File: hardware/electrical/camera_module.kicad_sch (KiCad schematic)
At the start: 19 parts, among them J5 FFC, Q7 AO3401A, U3 TLV70028DCKR, U9 TLV70012DCKR, X2 SG-8018CA 24.0000M-TJHPA3

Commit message: Component selection
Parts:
- C44, C52, C53: footprint (none) -> Capacitor_SMD:C_0402_1005Metric; LCSC Part # (none) -> C1525; Mfr (none) -> Samsung Electro-Mechanics; Mfr. Part # (none) -> CL05B104KO5NNNC
- C45: footprint (none) -> Capacitor_SMD:C_0603_1608Metric; LCSC Part # (none) -> C1644; Mfr (none) -> Samsung Electro-Mechanics; Mfr. Part # (none) -> CL10C150JB8NNNC
- C46, C47, C48, C49: footprint Capacitor_SMD:C_1206_3216Metric -> Capacitor_SMD:C_0402_1005Metric; LCSC Part # (none) -> C52923; Mfr (none) -> Samsung Electro-Mechanics; Mfr. Part # (none) -> CL05A105KA5NQNC
- C54: value DNP/100n -> 100n; footprint (none) -> Capacitor_SMD:C_0402_1005Metric; LCSC Part # (none) -> C1525; Mfr (none) -> Samsung Electro-Mechanics; Mfr. Part # (none) -> CL05B104KO5NNNC
- J5: LCSC Part # (none) -> C262643; Mfr (none) -> JUSHUO; Mfr. Part # (none) -> AFC07-S24ECA-00
- JP3: now left out of the parts list
- Q7: LCSC Part # (none) -> C15127; Mfr (none) -> Alpha & Omega Semicon; Mfr. Part # (none) -> AO3401A
- R28: footprint (none) -> Resistor_SMD:R_0402_1005Metric; LCSC Part # (none) -> C11702; Mfr (none) -> UNI-ROYAL(Uniroyal Elec); Mfr. Part # (none) -> 0402WGF1001TCE
- R29: footprint (none) -> Resistor_SMD:R_0402_1005Metric; LCSC Part # (none) -> C25744; Mfr (none) -> UNI-ROYAL(Uniroyal Elec); Mfr. Part # (none) -> 0402WGF1002TCE
- R30, R31: footprint (none) -> Resistor_SMD:R_0402_1005Metric; LCSC Part # (none) -> C25900; Mfr (none) -> UNI-ROYAL(Uniroyal Elec); Mfr. Part # (none) -> 0402WGF4701TCE
- U3: LCSC Part # (none) -> C398921; Mfr (none) -> Texas Instruments; Mfr. Part # (none) -> TLV70028DCKR
- U9: LCSC Part # (none) -> C96219; Mfr (none) -> Texas Instruments; Mfr. Part # (none) -> TLV70012DCKR
- X2: value SG-8018CA 24.0000M-TJHPA3 -> SG-8018CA 24.0000M-TJHPA3r; footprint Oscillator:Oscillator_SMD_SeikoEpson_SG8002CA-4Pin_7.0x5.0mm -> Oscillator:Oscillator_SMD_SeikoEpson_SG8002CA-4Pin_7.0x5.0mm_HandSoldering

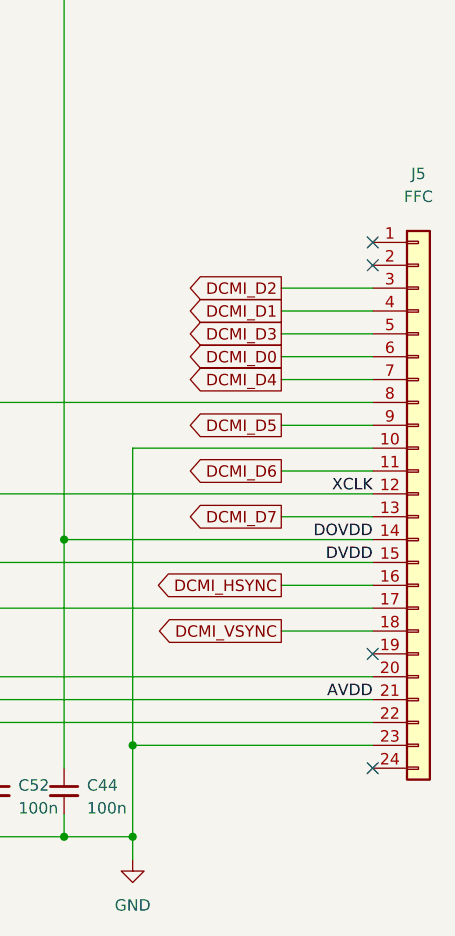
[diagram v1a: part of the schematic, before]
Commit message: Add Jushou AFC07-S24ECA-00 footprint and reverse J5 numbering to match camera cable
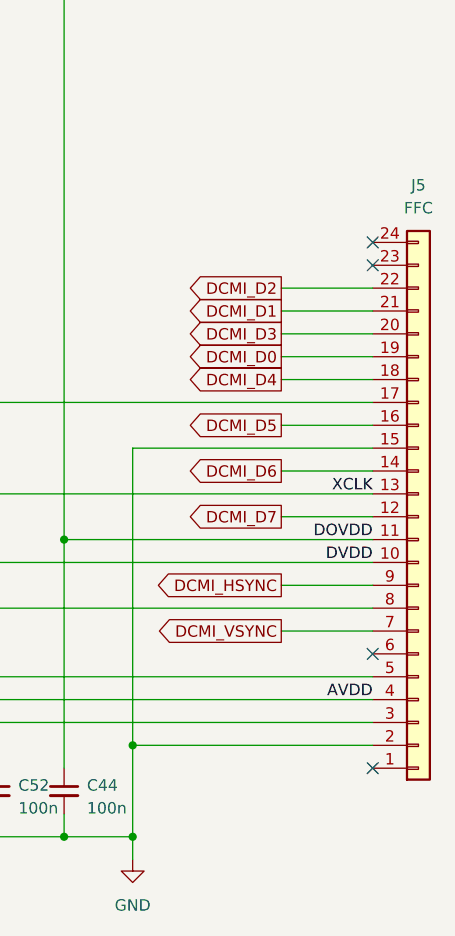
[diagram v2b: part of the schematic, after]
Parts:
- J5: footprint (none) -> 3885:Jushuo_AFC07-S24ECA-00_1x24-1MP_P0.50_Horizontal
- JP3: footprint (none) -> Jumper:SolderJumper-3_P1.3mm_Bridged12_Pad1.0x1.5mm
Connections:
- net AVDD: now also J5.4 (Pin_4); no longer J5.21 (Pin_21)
- net Cam_PWDN: now also J5.8 (Pin_8); no longer J5.17 (Pin_17)
- net Cam_SCL: now also J5.5 (Pin_5); no longer J5.20 (Pin_20)
- net Cam_SDA: now also J5.3 (Pin_3); no longer J5.22 (Pin_22)
- net DCMI_D0: now also J5.19 (Pin_19); no longer J5.6 (Pin_6)
- net DCMI_D1: now also J5.21 (Pin_21); no longer J5.4 (Pin_4)
- net DCMI_D2: now also J5.22 (Pin_22); no longer J5.3 (Pin_3)
- net DCMI_D3: now also J5.20 (Pin_20); no longer J5.5 (Pin_5)
- net DCMI_D4: now also J5.18 (Pin_18); no longer J5.7 (Pin_7)
- net DCMI_D5: now also J5.16 (Pin_16); no longer J5.9 (Pin_9)
- net DCMI_D6: now also J5.14 (Pin_14); no longer J5.11 (Pin_11)
- net DCMI_D7: now also J5.12 (Pin_12); no longer J5.13 (Pin_13)
- net DCMI_HSYNC: now also J5.9 (Pin_9); no longer J5.16 (Pin_16)
- net DCMI_PIXCLK: now also J5.17 (Pin_17); no longer J5.8 (Pin_8)
- net DCMI_VSYNC: now also J5.7 (Pin_7); no longer J5.18 (Pin_18)
- net DOVDD: now also J5.11 (Pin_11); no longer J5.14 (Pin_14)
- net DVDD: now also J5.10 (Pin_10); no longer J5.15 (Pin_15)
- net GND: now also J5.15 (Pin_15), J5.2 (Pin_2); no longer J5.10 (Pin_10), J5.23 (Pin_23)
- net XCLK: now also J5.13 (Pin_13); no longer J5.12 (Pin_12)
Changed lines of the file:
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@@
     )
   )
-  (symbol (lib_id "Connector_Generic:Conn_01x24") (at 255.27 113.03 0) (unit 1)
+  (symbol (lib_id "Connector_Generic:Conn_01x24") (at 255.27 115.57 0) (mirror x) (unit 1)
     (in_bom yes) (on_board yes) (dnp no)
-    (property "Reference" "J5" (at 255.27 77.47 0)
-      (effects (font (size 1.27 1.27)))
-    )
-    (property "Value" "FFC" (at 255.27 80.01 0)
-      (effects (font (size 1.27 1.27)))
-    )
-    (property "Footprint" "" (at 255.27 113.03 0)
-      (effects (font (size 1.27 1.27)) hide)
-    )
-    (property "Datasheet" "https://datasheet.lcsc.com/lcsc/1811021337_JUSHUO-AFC07-S24ECA-00_C262643.pdf" (at 255.27 113.03 0)
-      (effects (font (size 1.27 1.27)) hide)
-    )
-    (property "LCSC Part #" "C262643" (at 255.27 113.03 0)
-      (effects (font (size 1.27 1.27)) hide)
-    )
-    (property "Mfr" "JUSHUO" (at 255.27 113.03 0)
-      (effects (font (size 1.27 1.27)) hide)
-    )
-    (property "Mfr. Part #" "AFC07-S24ECA-00" (at 255.27 113.03 0)
+    (property "Reference" "J5" (at 255.27 78.74 0)
+      (effects (font (size 1.27 1.27)))
+    )
+    (property "Value" "FFC" (at 255.27 81.28 0)
+      (effects (font (size 1.27 1.27)))
+    )
+    (property "Footprint" "3885:Jushuo_AFC07-S24ECA-00_1x24-1MP_P0.50_Horizontal" (at 255.27 115.57 0)
+      (effects (font (size 1.27 1.27)) hide)
+    )
+    (property "Datasheet" "https://datasheet.lcsc.com/lcsc/1811021337_JUSHUO-AFC07-S24ECA-00_C262643.pdf" (at 255.27 115.57 0)
+      (effects (font (size 1.27 1.27)) hide)
+    )
+    (property "LCSC Part #" "C262643" (at 255.27 115.57 0)
+      (effects (font (size 1.27 1.27)) hide)
+    )
+    (property "Mfr" "JUSHUO" (at 255.27 115.57 0)
+      (effects (font (size 1.27 1.27)) hide)
+    )
+    (property "Mfr. Part #" "AFC07-S24ECA-00" (at 255.27 115.57 0)
       (effects (font (size 1.27 1.27)) hide)
     )
@@
       (effects (font (size 1.27 1.27)) (justify left) hide)
     )
-    (property "Footprint" "" (at 135.89 146.05 0)
-      (effects (font (size 1.27 1.27)) hide)
-    )
+    (property "Footprint" "Jumper:SolderJumper-3_P1.3mm_Bridged12_Pad1.0x1.5mm" (at 135.89 146.05 0)
+      (effects (font (size 1.27 1.27)) hide)
+    )
